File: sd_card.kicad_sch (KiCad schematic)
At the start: 18 parts, among them J5 Screw_Terminal_01x03, J701 DM3AT-SF-PEJM5_40_, U11 EMIF06-MSD02N16, U702 ADM2565EBRNZ

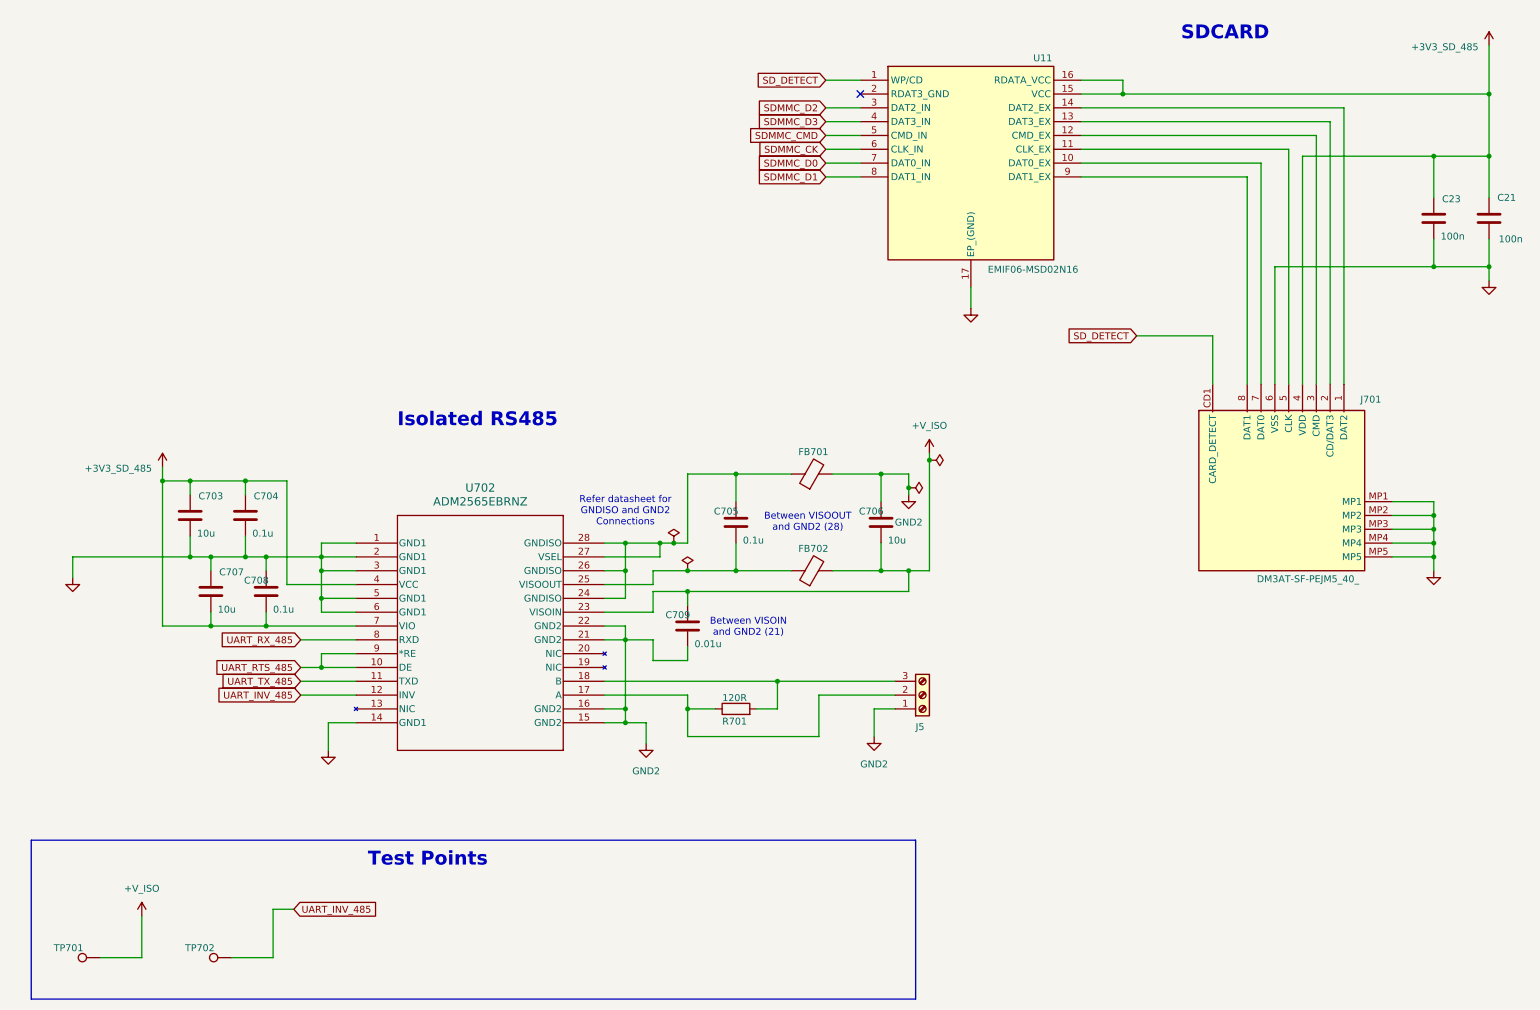
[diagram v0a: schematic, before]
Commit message: only usb powered
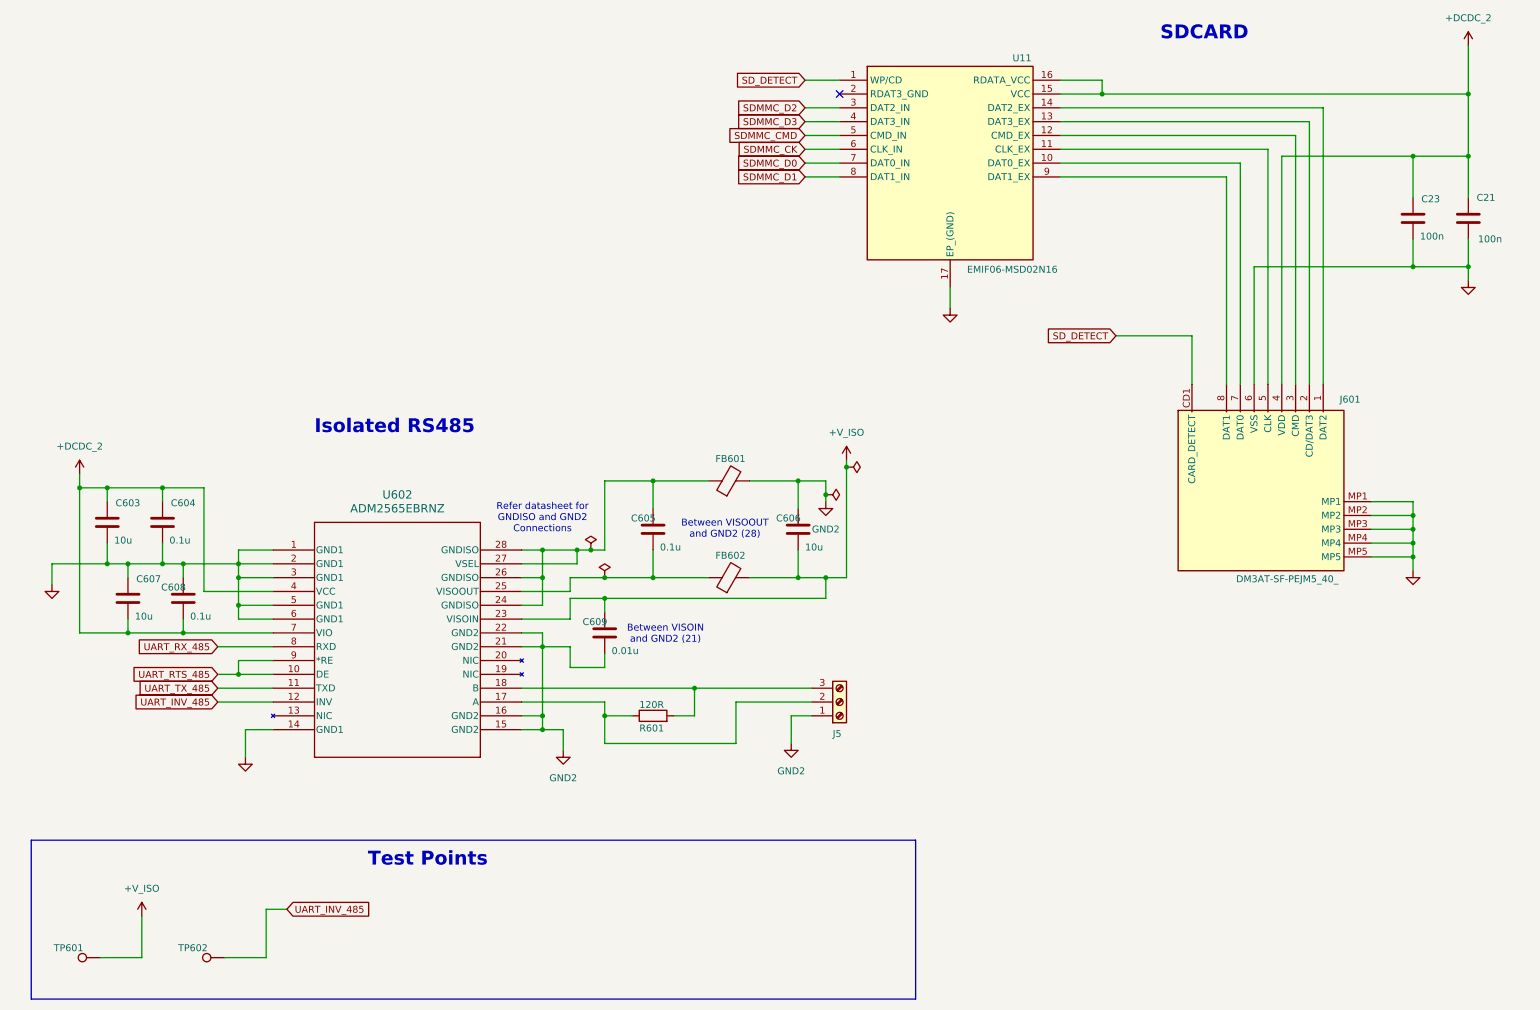
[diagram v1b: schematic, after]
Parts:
- renumbered C703 to C603, C704 to C604, C705 to C605, C706 to C606, C707 to C607, C708 to C608, C709 to C609, FB701 to FB601, FB702 to FB602, J701 to J601, R701 to R601, TP701 to TP601, TP702 to TP602, U702 to U602
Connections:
- net +3V3_SD_485 renamed +DCDC_2
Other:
- moved on the sheet: C21, C23, C603, C604, C605, C606, C607, C608, C609, FB601, FB602, J5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

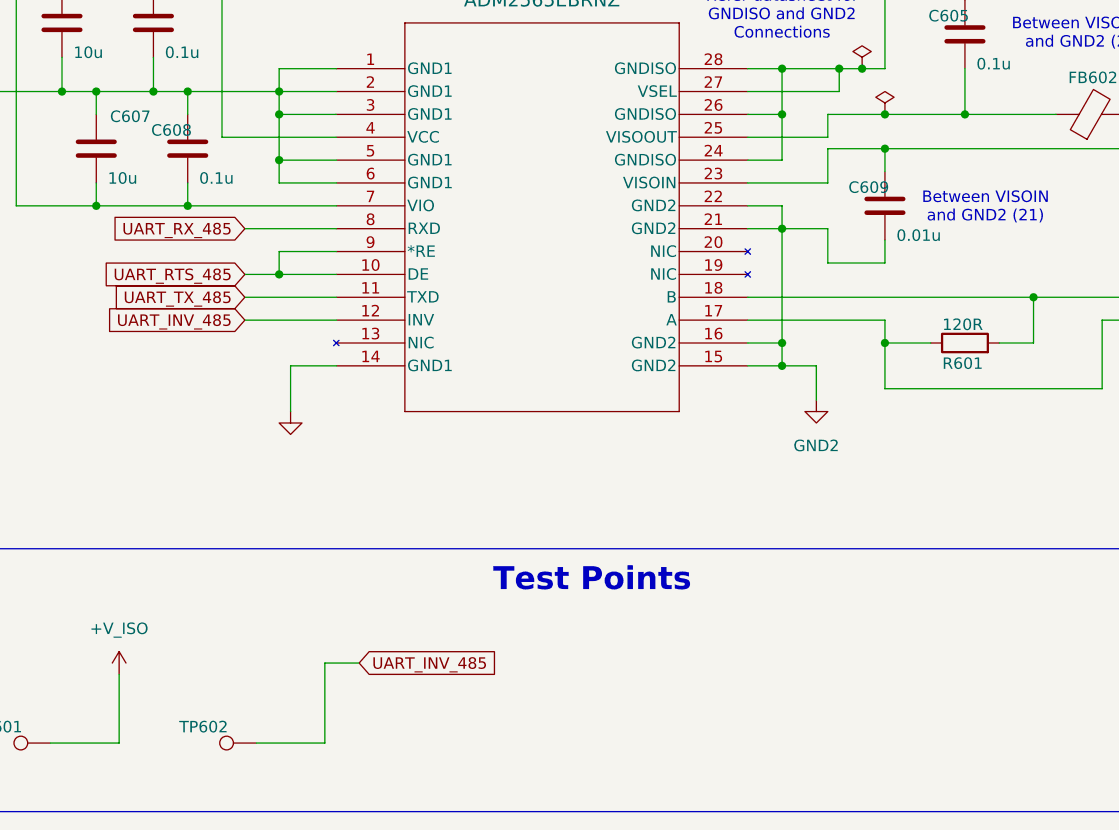
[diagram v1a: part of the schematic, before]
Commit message: components with distributor links added
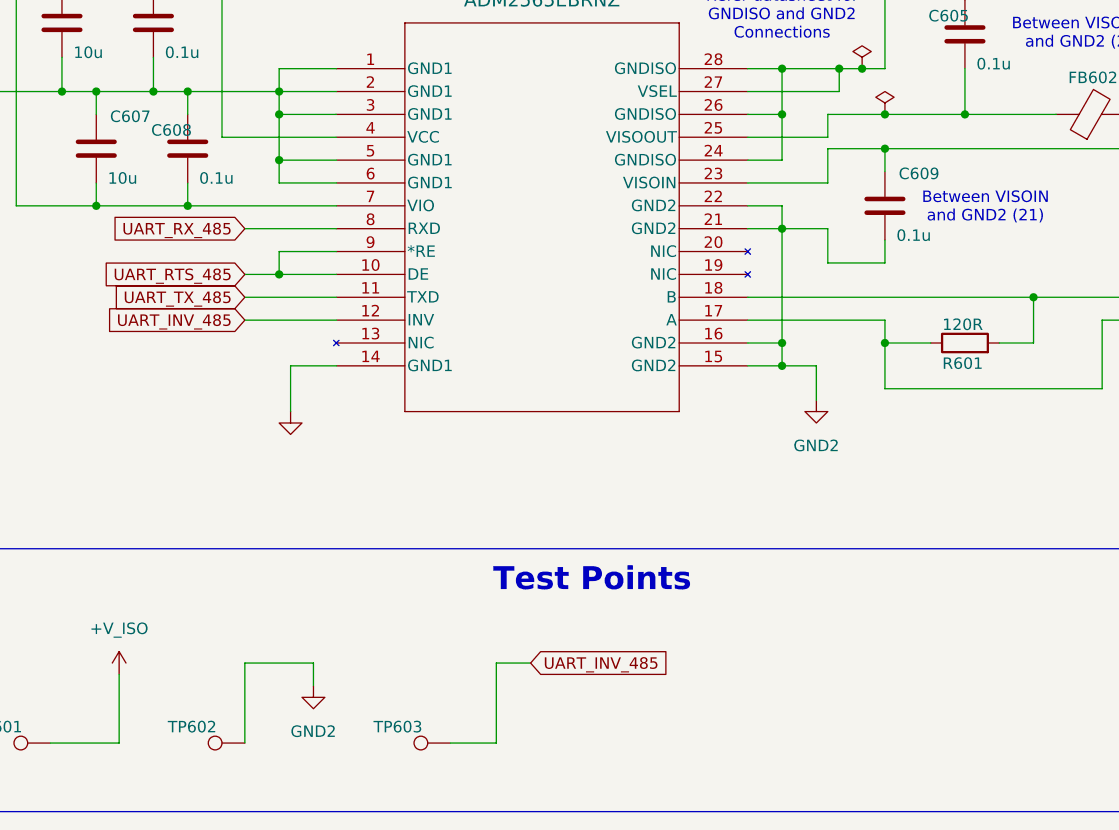
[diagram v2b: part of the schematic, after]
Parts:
- added TP602: TestPoint, EMS:5000, symbol Connector:TestPoint
- C21, C23: Distributor_Link (none) -> https://www.mouser.com/ProductDetail/KYOCERA-AVX/04023C104K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; Manufacturer_Name (none) -> KYOCERA AVX; Manufacturer_Part_Number (none) -> 04023C104KAT2A
- C603, C606, C607: footprint Capacitor_SMD:C_0402_1005Metric -> Capacitor_SMD:C_0603_1608Metric; Distributor_Link (none) -> https://www.mouser.com/ProductDetail/KYOCERA-AVX/KGM15CR51A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; Manufacturer_Name (none) -> KYOCERA AVX; Manufacturer_Part_Number (none) -> KGM15CR51A106KT
- C604, C605, C608: Distributor_Link (none) -> https://www.mouser.com/ProductDetail/KYOCERA-AVX/04023D104J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; Manufacturer_Name (none) -> KYOCERA AVX; Manufacturer_Part_Number (none) -> 04023D104JAT2A
- C609: value 0.01u -> 0.1u; Distributor_Link (none) -> https://www.mouser.com/ProductDetail/KYOCERA-AVX/04023D104J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; Manufacturer_Name (none) -> KYOCERA AVX; Manufacturer_Part_Number (none) -> 04023D104JAT2A
- FB601, FB602: Distributor_Link (none) -> https://www.mouser.com/ProductDetail/Murata-Electronics/BLM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; Manufacturer_Name (none) -> Murata Electronics; Manufacturer_Part_Number (none) -> BLM15HD182SN1D
- J5: footprint TerminalBlock_Phoenix:TerminalBlock_Phoenix_MKDS-1,5-3_1x03_P5.00mm_Horizontal -> TerminalBlock_Phoenix:TerminalBlock_Phoenix_MKDS-1,5-3-5.08_1x03_P5.08mm_Horizontal; Distributor_Link (none) -> https://www.mouser.com/ProductDetail/Phoenix-Contact/154812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; Manufacturer_Name (none) -> Phoenix Contact; Manufacturer_Part_Number (none) -> 1548129
- J601: Distributor_Link (none) -> https://www.mouser.co.uk/ProductDetail/Hirose-Connector/DM3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
- R601: Distributor_Link (none) -> https://www.mouser.com/ProductDetail/ROHM-Semiconductor/SFR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; Manufacturer_Name (none) -> ROHM Semiconductor; Manufacturer_Part_Number (none) -> SFR01MZPF1200
- TP601: footprint TestPoint:TestPoint_Loop_D3.50mm_Drill1.4mm_Beaded -> EMS:5000; Distributor_Link (none) -> https://www.mouser.com/ProductDetail/Keystone-Electronics/5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; Manufacturer_Name (none) -> Keystone Electronics; Manufacturer_Part_Number (none) -> 5000
- TP603: renamed from TP602; footprint TestPoint:TestPoint_Loop_D3.50mm_Drill1.4mm_Beaded -> EMS:5000; Distributor_Link (none) -> https://www.mouser.com/ProductDetail/Keystone-Electronics/5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; Manufacturer_Name (none) -> Keystone Electronics; Manufacturer_Part_Number (none) -> 5000
- U11: Distributor_Link (none) -> https://www.mouser.co.uk/ProductDetail/STMicroelectronics/E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
- U602: Distributor_Link (none) -> https://www.mouser.com/ProductDetail/Analog-Devices/ADM2565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; Manufacturer_Name (none) -> Analog Devices; Manufacturer_Part_Number (none) -> ADM2565EBRNZ
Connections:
- net GND2: now also TP602.1
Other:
- moved on the sheet: TP603

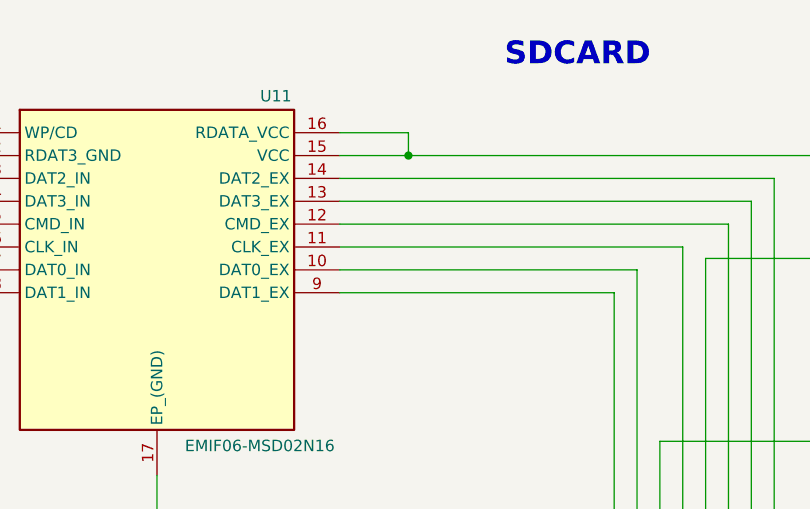
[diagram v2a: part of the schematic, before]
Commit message: minor improvements to net labeling
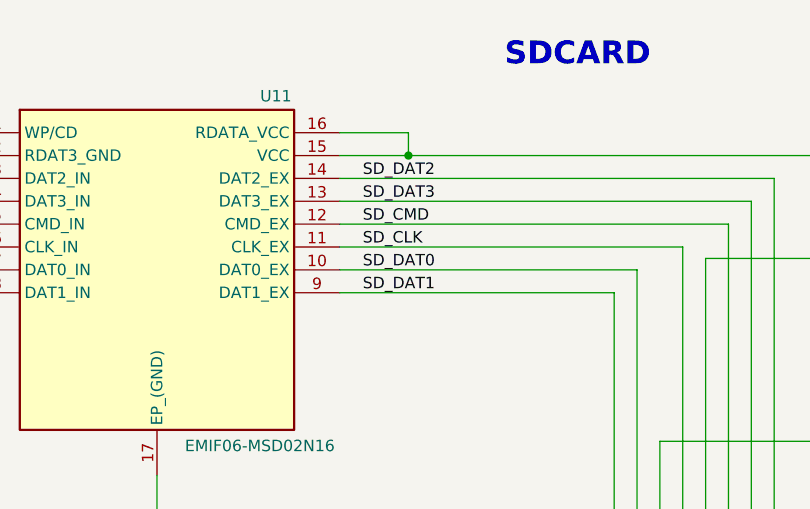
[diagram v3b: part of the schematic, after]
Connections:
- net SD_DAT0: now reaches J601.7 (DAT0), U11.10 (DAT0_EX)
- net SD_CLK: now reaches J601.5 (CLK), U11.11 (CLK_EX)
- net SD_CMD: now reaches J601.3 (CMD), U11.12 (CMD_EX)
- net SD_DAT3: now reaches J601.2 (CD/DAT3), U11.13 (DAT3_EX)
- net SD_DAT2: now reaches J601.1 (DAT2), U11.14 (DAT2_EX)
- net SD_DAT1: now reaches J601.8 (DAT1), U11.9 (DAT1_EX)
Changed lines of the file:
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@@
+		)
+	)
+	(label "SD_DAT0"
+		(at 204.47 43.18 0)
+		(fields_autoplaced yes)
+		(effects
+			(font
+				(size 1.27 1.27)
+			)
+			(justify left bottom)
+		)
+	)
+	(label "SD_DAT2"
+		(at 204.47 33.02 0)
+		(fields_autoplaced yes)
+		(effects
+			(font
+				(size 1.27 1.27)
+			)
+			(justify left bottom)
+		)
+	)
+	(label "SD_DAT3"
+		(at 204.47 35.56 0)
+		(fields_autoplaced yes)
+		(effects
+			(font
+				(size 1.27 1.27)
+			)
+			(justify left bottom)
+		)
+	)
+	(label "SD_CLK"
+		(at 204.47 40.64 0)
+		(fields_autoplaced yes)
+		(effects
+			(font
+				(size 1.27 1.27)
+			)
+			(justify left bottom)
+		)
+	)
+	(label "SD_DAT1"
+		(at 204.47 45.72 0)
+		(fields_autoplaced yes)
+		(effects
+			(font
+				(size 1.27 1.27)
+			)
+			(justify left bottom)
+		)
+	)
+	(label "SD_CMD"
+		(at 204.47 38.1 0)
+		(fields_autoplaced yes)
+		(effects
+			(font
+				(size 1.27 1.27)
+			)
+			(justify left bottom)
 		)
 	)

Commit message: finalized design v1.0.0
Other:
- note added: "[4] Interfacing"
- company: (none) -> Manufacturing Innovation Network Laboratory (MINLab)
- title: (none) -> Energy Monitoring System
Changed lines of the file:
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@@
 	(generator_version "8.0")
 	(paper "A4")
+	(title_block
+		(title "Energy Monitoring System")
+		(rev "v1.0.0")
+		(company "Manufacturing Innovation Network Laboratory (MINLab)")
+		(comment 1 "Developed by Vignesh Selvaraj")
+	)
 	(junction
 		(at 276.86 30.48)
@@
 			)
 		)
+	)
+	(text "[4] Interfacing"
+		(exclude_from_sim no)
+		(at 36.576 19.558 0)
+		(effects
+			(font
+				(size 3.81 3.81)
+				(thickness 1.016)
+				(bold yes)
+			)
+		)
